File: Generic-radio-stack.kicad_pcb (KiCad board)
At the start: 2 copper layers, 1 part

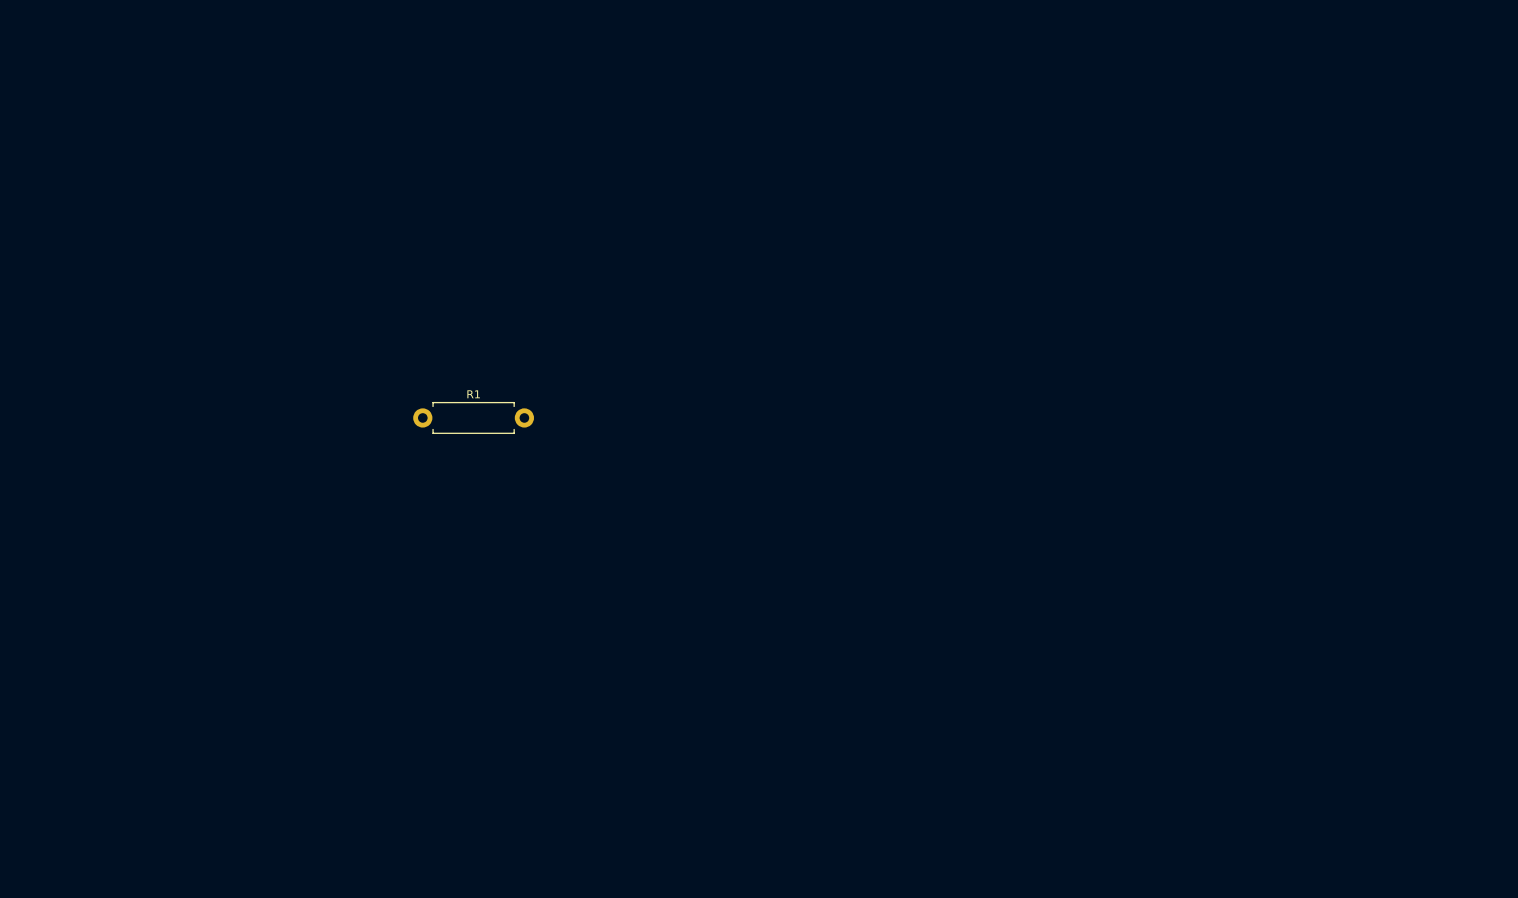
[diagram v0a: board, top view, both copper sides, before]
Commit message: Use native KiBot replacement for date and version
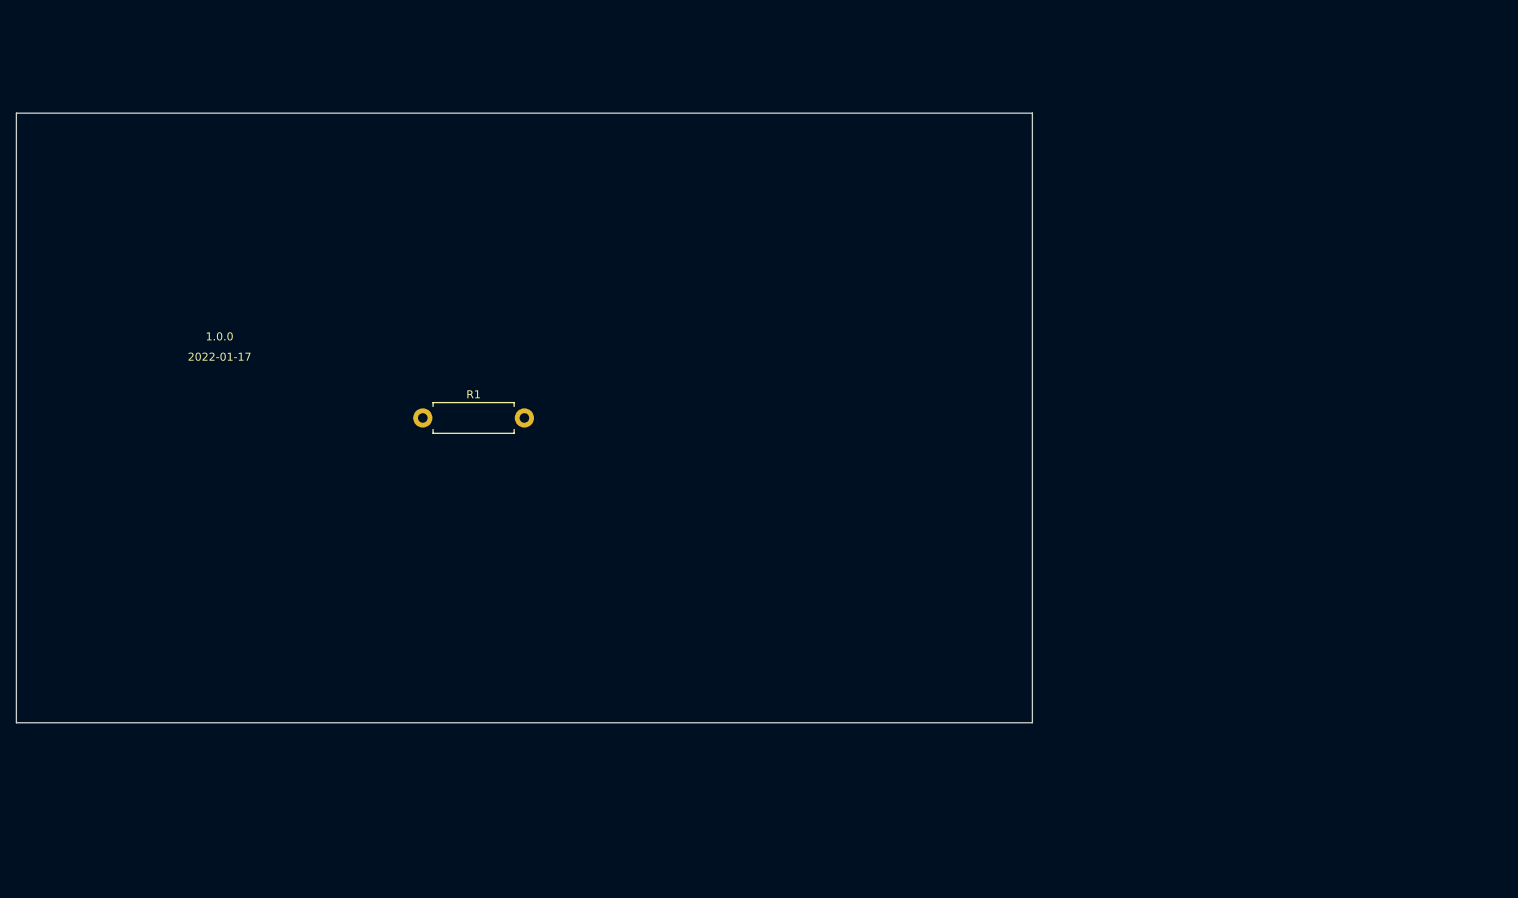
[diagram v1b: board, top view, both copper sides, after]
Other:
- board outline added: 127 x 76.2 mm
- board text added: "1.0.0"
- board text added: "2022-01-17"
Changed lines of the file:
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@@
   )
   (paper "A4")
+  (title_block
+    (date "2022-01-17")
+    (rev "1.0.0")
+  )
   (layers
     (0 "F.Cu" signal)
@@
     )
   )
+  (gr_line (start 50.8 50.8) (end 50.8 127) (layer "Edge.Cuts") (width 0.1))
+  (gr_line (start 177.8 50.8) (end 50.8 50.8) (layer "Edge.Cuts") (width 0.1))
+  (gr_line (start 177.8 127) (end 177.8 50.8) (layer "Edge.Cuts") (width 0.1))
+  (gr_line (start 50.8 127) (end 177.8 127) (layer "Edge.Cuts") (width 0.1))
+  (gr_text "2022-01-17" (at 76.2 81.28) (layer "F.SilkS")
+    (effects (font (size 1 1) (thickness 0.15)))
+  )
+  (gr_text "1.0.0" (at 76.2 78.74) (layer "F.SilkS")
+    (effects (font (size 1 1) (thickness 0.15)))
+  )
+  (gr_text "" (at 76.2 76.2) (layer "F.SilkS")
+    (effects (font (size 1 1) (thickness 0.15)))
+  )
 )

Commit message: Add placeholders
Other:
- board text added: "@date@"
- board text added: "@version@"
- board text removed: "1.0.0"
- board text removed: "2022-01-17"
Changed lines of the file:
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@@
   (title_block
     (date "2022-01-17")
-    (rev "1.0.0")
+    (rev "@version@")
   )
   (layers
@@
   (gr_line (start 177.8 127) (end 177.8 50.8) (layer "Edge.Cuts") (width 0.1))
   (gr_line (start 50.8 127) (end 177.8 127) (layer "Edge.Cuts") (width 0.1))
-  (gr_text "2022-01-17" (at 76.2 81.28) (layer "F.SilkS")
+  (gr_text "@date@" (at 76.2 81.28) (layer "F.SilkS")
     (effects (font (size 1 1) (thickness 0.15)))
   )
-  (gr_text "1.0.0" (at 76.2 78.74) (layer "F.SilkS")
+  (gr_text "@version@" (at 76.2 78.74) (layer "F.SilkS")
     (effects (font (size 1 1) (thickness 0.15)))
   )

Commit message: Custom component for six digit display
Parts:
- removed R1: 10k, Resistor_THT:R_Axial_DIN0411_L9.9mm_D3.6mm_P12.70mm_Horizontal
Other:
- board outline removed
- board text removed: "@date@"
- board text removed: "@version@"
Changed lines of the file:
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@@
   )
   (net 0 "")
-  (net 1 "unconnected-(R1-Pad1)")
-  (net 2 "unconnected-(R1-Pad2)")
-  (footprint "Resistor_THT:R_Axial_DIN0411_L9.9mm_D3.6mm_P12.70mm_Horizontal" (layer "F.Cu")
-    (at 101.6 88.9)
-    (descr "Resistor, Axial_DIN0411 series, Axial, Horizontal, pin pitch=12.7mm, 1W, length*diameter=9.9*3.6mm^2")
-    (tags "Resistor Axial_DIN0411 series Axial Horizontal pin pitch 12.7mm 1W length 9.9mm diameter 3.6mm")
-    (property "Sheetfile" "Generic-radio-stack.kicad_sch")
-    (property "Sheetname" "")
-    (attr through_hole)
-    (fp_text reference "R1" (at 6.35 -2.92) (layer "F.SilkS")
-      (effects (font (size 1 1) (thickness 0.15)))
-    )
-    (fp_text value "10k" (at 6.35 2.92) (layer "F.Fab")
-      (effects (font (size 1 1) (thickness 0.15)))
-    )
-    (fp_text user "${REFERENCE}" (at 6.35 0) (layer "F.Fab")
-      (effects (font (size 1 1) (thickness 0.15)))
-    )
-    (fp_line (start 1.28 -1.92) (end 11.42 -1.92) (layer "F.SilkS") (width 0.12))
-    (fp_line (start 1.28 1.92) (end 11.42 1.92) (layer "F.SilkS") (width 0.12))
-    (fp_line (start 1.28 1.44) (end 1.28 1.92) (layer "F.SilkS") (width 0.12))
-    (fp_line (start 11.42 -1.92) (end 11.42 -1.44) (layer "F.SilkS") (width 0.12))
-    (fp_line (start 1.28 -1.44) (end 1.28 -1.92) (layer "F.SilkS") (width 0.12))
-    (fp_line (start 11.42 1.92) (end 11.42 1.44) (layer "F.SilkS") (width 0.12))
-    (fp_line (start 14.15 2.05) (end 14.15 -2.05) (layer "F.CrtYd") (width 0.05))
-    (fp_line (start 14.15 -2.05) (end -1.45 -2.05) (layer "F.CrtYd") (width 0.05))
-    (fp_line (start -1.45 2.05) (end 14.15 2.05) (layer "F.CrtYd") (width 0.05))
-    (fp_line (start -1.45 -2.05) (end -1.45 2.05) (layer "F.CrtYd") (width 0.05))
-    (fp_line (start 0 0) (end 1.4 0) (layer "F.Fab") (width 0.1))
-    (fp_line (start 11.3 1.8) (end 11.3 -1.8) (layer "F.Fab") (width 0.1))
-    (fp_line (start 1.4 -1.8) (end 1.4 1.8) (layer "F.Fab") (width 0.1))
-    (fp_line (start 1.4 1.8) (end 11.3 1.8) (layer "F.Fab") (width 0.1))
-    (fp_line (start 12.7 0) (end 11.3 0) (layer "F.Fab") (width 0.1))
-    (fp_line (start 11.3 -1.8) (end 1.4 -1.8) (layer "F.Fab") (width 0.1))
-    (pad "1" thru_hole circle (at 0 0) (size 2.4 2.4) (drill 1.2) (layers *.Cu *.Mask)
-      (net 1 "unconnected-(R1-Pad1)") (pintype "passive"))
-    (pad "2" thru_hole oval (at 12.7 0) (size 2.4 2.4) (drill 1.2) (layers *.Cu *.Mask)
-      (net 2 "unconnected-(R1-Pad2)") (pintype "passive"))
-    (model "${KICAD6_3DMODEL_DIR}/Resistor_THT.3dshapes/R_Axial_DIN0411_L9.9mm_D3.6mm_P12.70mm_Horizontal.wrl"
-      (offset (xyz 0 0 0))
-      (scale (xyz 1 1 1))
-      (rotate (xyz 0 0 0))
-    )
-  )
-  (gr_line (start 50.8 50.8) (end 50.8 127) (layer "Edge.Cuts") (width 0.1))
-  (gr_line (start 177.8 50.8) (end 50.8 50.8) (layer "Edge.Cuts") (width 0.1))
-  (gr_line (start 177.8 127) (end 177.8 50.8) (layer "Edge.Cuts") (width 0.1))
-  (gr_line (start 50.8 127) (end 177.8 127) (layer "Edge.Cuts") (width 0.1))
-  (gr_text "@date@" (at 76.2 81.28) (layer "F.SilkS")
-    (effects (font (size 1 1) (thickness 0.15)))
-  )
-  (gr_text "@version@" (at 76.2 78.74) (layer "F.SilkS")
-    (effects (font (size 1 1) (thickness 0.15)))
-  )
-  (gr_text "" (at 76.2 76.2) (layer "F.SilkS")
-    (effects (font (size 1 1) (thickness 0.15)))
-  )
 )

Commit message: More footprint updates
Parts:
- added C1: 10uF, Generic-radio-stack:Perfect_0402, F.Cu at (215.9, 109.2)
- added C10: 100nF, Generic-radio-stack:Perfect_0402, F.Cu at (62.0, 53.2)
- added C11: 10uF, Generic-radio-stack:Perfect_0402, F.Cu at (65.2, 140.7)
- added C12: 100nF, Generic-radio-stack:Perfect_0402, F.Cu at (62.0, 140.7)
- added C13: 10uF, Generic-radio-stack:Perfect_0402, F.Cu at (190.4, 80.8)
- added C14: 100nF, Generic-radio-stack:Perfect_0402, F.Cu at (187.3, 80.8)
- added C15: 10uF, Generic-radio-stack:Perfect_0402, F.Cu at (133.2, 102.9)
- added C16: 100nF, Generic-radio-stack:Perfect_0402, F.Cu at (130.1, 102.9)
- added C17: 10uF, Generic-radio-stack:Perfect_0402, F.Cu at (133.2, 80.8)
- added C18: 100nF, Generic-radio-stack:Perfect_0402, F.Cu at (130.1, 80.8)
- added C19: 27p, Generic-radio-stack:Perfect_0402, F.Cu at (196.1, 140.3)
- added C2: 10uF, Generic-radio-stack:Perfect_0402, F.Cu at (193.6, 119.2)
- added C20: 27p, Generic-radio-stack:Perfect_0402, F.Cu at (215.3, 126.9)
- added C21: 100nF, Generic-radio-stack:Perfect_0402, F.Cu at (199.2, 140.3)
- added C22: 100nF, Generic-radio-stack:Perfect_0402, F.Cu at (196.1, 138.3)
- added C23: 1uF, Generic-radio-stack:Perfect_0402, F.Cu at (205.4, 136.2)
- added C24: 1uF, Generic-radio-stack:Perfect_0402, F.Cu at (208.6, 134.1)
- added C25: 100nF, Generic-radio-stack:Perfect_0402, F.Cu at (218.5, 124.8)
- added C26: 100nF, Generic-radio-stack:Perfect_0402, F.Cu at (212.2, 128.9)
- added C27: 100nF, Generic-radio-stack:Perfect_0402, F.Cu at (212.2, 126.9)
- added C28: 100nF, Generic-radio-stack:Perfect_0402, F.Cu at (202.3, 134.1)
- added C29: 100nF, Generic-radio-stack:Perfect_0402, F.Cu at (202.3, 138.2)
- added C3: 10uF, Generic-radio-stack:Perfect_0402, F.Cu at (133.2, 53.2)
- added C30: 100nF, Generic-radio-stack:Perfect_0402, F.Cu at (202.3, 136.2)
- added C31: 100nF, Generic-radio-stack:Perfect_0402, F.Cu at (202.3, 140.3)
- added C32: 100nF, Generic-radio-stack:Perfect_0402, F.Cu at (199.2, 142.4)
- added C4: 100nF, Generic-radio-stack:Perfect_0402, F.Cu at (130.1, 53.2)
- added C5: 10uF, Generic-radio-stack:Perfect_0402, F.Cu at (65.2, 110.6)
- added C6: 100nF, Generic-radio-stack:Perfect_0402, F.Cu at (62.0, 110.6)
- added C7: 10uF, Generic-radio-stack:Perfect_0402, F.Cu at (65.2, 81.9)
- added C8: 100nF, Generic-radio-stack:Perfect_0402, F.Cu at (62.0, 81.9)
- added C9: 10uF, Generic-radio-stack:Perfect_0402, F.Cu at (65.2, 53.2)
- added D1: GREEN, LED_THT:LED_D5.0mm, F.Cu at (209.3, 107.1)
- added D2: GREEN, LED_THT:LED_D5.0mm, F.Cu at (219.2, 98.9)
- added D3: GREEN, LED_THT:LED_D5.0mm, F.Cu at (197.9, 116.6)
- added D4: GREEN, LED_THT:LED_D5.0mm, F.Cu at (205.4, 116.6)
- added D5: LED_Small, Generic-radio-stack:LED_0603_1608Metric, F.Cu at (216.4, 104.9)
- added ENC1: EC11EBB24C03, Generic-radio-stack:ALPS-EC11EBB24C03-0, F.Cu at (135.7, 129.0)
- added ENC2: EC11EBB24C03, Generic-radio-stack:ALPS-EC11EBB24C03-0, F.Cu at (203.7, 51.6)
- added J1: USB_B_Mini, Generic-radio-stack:USB_B_Mini_Amphenol_UE25BE5510H, F.Cu at (190.6, 115.5)
- added J2: Conn_01x02, Connector_PinHeader_2.54mm:PinHeader_1x02_P2.54mm_Vertical, F.Cu at (198.4, 132.4)
- added R1: 1k, Generic-radio-stack:Perfect_0402, F.Cu at (220.2, 103.7)
- added R10: R_Small, Generic-radio-stack:Perfect_0402, F.Cu at (130.1, 57.8)
- added R11: R_Small, Generic-radio-stack:Perfect_0402, F.Cu at (62.0, 115.3)
- added R12: R_Small, Generic-radio-stack:Perfect_0402, F.Cu at (62.0, 86.5)
- added R13: R_Small, Generic-radio-stack:Perfect_0402, F.Cu at (62.0, 57.8)
- added R14: R_Small, Generic-radio-stack:Perfect_0402, F.Cu at (62.0, 146.5)
- added R15: R_Small, Generic-radio-stack:Perfect_0402, F.Cu at (187.3, 86.5)
- added R16: R_Small, Generic-radio-stack:Perfect_0402, F.Cu at (130.1, 108.7)
- added R17: R_Small, Generic-radio-stack:Perfect_0402, F.Cu at (130.1, 86.5)
- added R18: 10k, Generic-radio-stack:Perfect_0402, F.Cu at (144.4, 120.3)
- added R19: 10k, Generic-radio-stack:Perfect_0402, F.Cu at (150.7, 118.3)
- added R2: 1k, Generic-radio-stack:Perfect_0402, F.Cu at (187.3, 119.2)
- added R20: 10k, Generic-radio-stack:Perfect_0402, F.Cu at (144.4, 118.3)
- added R21: 10k, Generic-radio-stack:Perfect_0402, F.Cu at (147.5, 118.3)
- added R22: 10k, Generic-radio-stack:Perfect_0402, F.Cu at (130.1, 138.9)
- added R23: 10k, Generic-radio-stack:Perfect_0402, F.Cu at (212.4, 42.9)
- added R24: 10k, Generic-radio-stack:Perfect_0402, F.Cu at (218.7, 40.9)
- added R25: 10k, Generic-radio-stack:Perfect_0402, F.Cu at (212.4, 40.9)
- added R26: 10k, Generic-radio-stack:Perfect_0402, F.Cu at (215.6, 40.9)
- added R27: 10k, Generic-radio-stack:Perfect_0402, F.Cu at (198.1, 61.5)
- added R28: 1k, Generic-radio-stack:Perfect_0402, F.Cu at (208.6, 136.2)
- added R29: 27, Generic-radio-stack:Perfect_0402, F.Cu at (212.2, 131.0)
- added R3: 1k, Generic-radio-stack:Perfect_0402, F.Cu at (212.0, 111.9)
- added R30: 27, Generic-radio-stack:Perfect_0402, F.Cu at (205.4, 134.1)
- added R31: 197, Generic-radio-stack:Perfect_0402, F.Cu at (211.8, 134.1)
- added R32: 197, Generic-radio-stack:Perfect_0402, F.Cu at (196.1, 142.4)
- added R33: 1k, Generic-radio-stack:Perfect_0402, F.Cu at (199.2, 138.3)
- added R34: 197, Generic-radio-stack:Perfect_0402, F.Cu at (215.3, 128.9)
- added R35: 10k, Generic-radio-stack:Perfect_0402, F.Cu at (205.5, 138.2)
- added R36: 310, Generic-radio-stack:Perfect_0402, F.Cu at (212.2, 124.8)
- added R37: 310, Generic-radio-stack:Perfect_0402, F.Cu at (202.3, 142.3)
- added R38: 310, Generic-radio-stack:Perfect_0402, F.Cu at (215.3, 124.8)
- added R4: 1k, Generic-radio-stack:Perfect_0402, F.Cu at (215.9, 107.2)
- added R5: 1k, Generic-radio-stack:Perfect_0402, F.Cu at (228.9, 98.2)
- added R6: 1k, Generic-radio-stack:Perfect_0402, F.Cu at (225.8, 98.2)
- added R7: 1k, Generic-radio-stack:Perfect_0402, F.Cu at (225.8, 96.1)
- added R8: 1k, Generic-radio-stack:Perfect_0402, F.Cu at (228.9, 96.1)
- added R9: 1k, Generic-radio-stack:Perfect_0402, F.Cu at (190.4, 119.2)
- added SW1: SW_Push_LED, Generic-radio-stack:SW_PUSH_6mm, F.Cu at (187.8, 106.1)
- added SW2: SW_Push_LED, Generic-radio-stack:SW_PUSH_6mm, F.Cu at (198.3, 97.3)
- added SW3: SW_Push_LED, Generic-radio-stack:SW_PUSH_6mm, F.Cu at (198.3, 106.1)
- added SW4: SW_Push_LED, Generic-radio-stack:SW_PUSH_6mm, F.Cu at (187.8, 97.3)
- added U1: NCP1117-3.3_SOT223, Package_TO_SOT_SMD:SOT-223-3_TabPin2, F.Cu at (211.8, 99.2)
- added U10: MAX7219, Package_SO:SOIC-24W_7.5x15.4mm_P1.27mm, F.Cu at (105.6, 137.0)
- added U11: 5_digit_7_segment_display, Generic-radio-stack:5 digit (3+2) 7 segment LED display, F.Cu at (79.8, 134.1)
- added U12: MAX7219, Package_SO:SOIC-24W_7.5x15.4mm_P1.27mm, F.Cu at (230.8, 77.0)
- added U13: 5_digit_7_segment_display, Generic-radio-stack:5 digit (3+2) 7 segment LED display, F.Cu at (205.0, 74.1)
- added U14: MAX7219, Package_SO:SOIC-24W_7.5x15.4mm_P1.27mm, F.Cu at (173.6, 99.2)
- added U15: 5_digit_7_segment_display, Generic-radio-stack:5 digit (3+2) 7 segment LED display, F.Cu at (147.8, 96.2)
- added U16: MAX7219, Package_SO:SOIC-24W_7.5x15.4mm_P1.27mm, F.Cu at (173.6, 77.0)
- added U17: 5_digit_7_segment_display, Generic-radio-stack:5 digit (3+2) 7 segment LED display, F.Cu at (147.8, 74.1)
- added U18: RP2040, RP2040_minimal:RP2040-QFN-56, F.Cu at (206.0, 128.5)
- added U19: LSF0204PWR, Package_SO:TSSOP-14_4.4x5mm_P0.65mm, F.Cu at (190.1, 140.1)
- added U2: MAX7219, Package_SO:SOIC-24W_7.5x15.4mm_P1.27mm, F.Cu at (181.2, 48.3)
- added U20: W25Q128JVS, Package_SO:SOIC-8_5.23x5.23mm_P1.27mm, F.Cu at (190.9, 133.5)
- added U3: 6_digit_7_segment_display_1, Generic-radio-stack:6 digit (3+3) 7 segment LED display, F.Cu at (151.6, 45.4)
- added U4: MAX7219, Package_SO:SOIC-24W_7.5x15.4mm_P1.27mm, F.Cu at (113.1, 105.8)
- added U5: 6_digit_7_segment_display_1, Generic-radio-stack:6 digit (3+3) 7 segment LED display, F.Cu at (83.6, 102.8)
- added U6: MAX7219, Package_SO:SOIC-24W_7.5x15.4mm_P1.27mm, F.Cu at (113.1, 77.0)
- added U7: 6_digit_7_segment_display_1, Generic-radio-stack:6 digit (3+3) 7 segment LED display, F.Cu at (83.6, 74.1)
- added U8: MAX7219, Package_SO:SOIC-24W_7.5x15.4mm_P1.27mm, F.Cu at (113.1, 48.3)
- added U9: 6_digit_7_segment_display_1, Generic-radio-stack:6 digit (3+3) 7 segment LED display, F.Cu at (83.6, 45.4)
- added Y1: ABLS-12.000MHZ-B4-T, RP2040_minimal:Crystal_SMD_HC49-US, F.Cu at (193.5, 127.0)
